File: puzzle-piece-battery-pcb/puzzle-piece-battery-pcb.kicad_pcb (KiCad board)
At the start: 2 copper layers, 27 x 27 mm, 18 parts, among them J1 Lipo, J2 INPUT, J3 OUTPUT, J4 GND Rivet, J5 5V Rivet, J6 3.3V Rivet, U2 MCP73831T-2ACI/OT, U3 LM3480-3.3

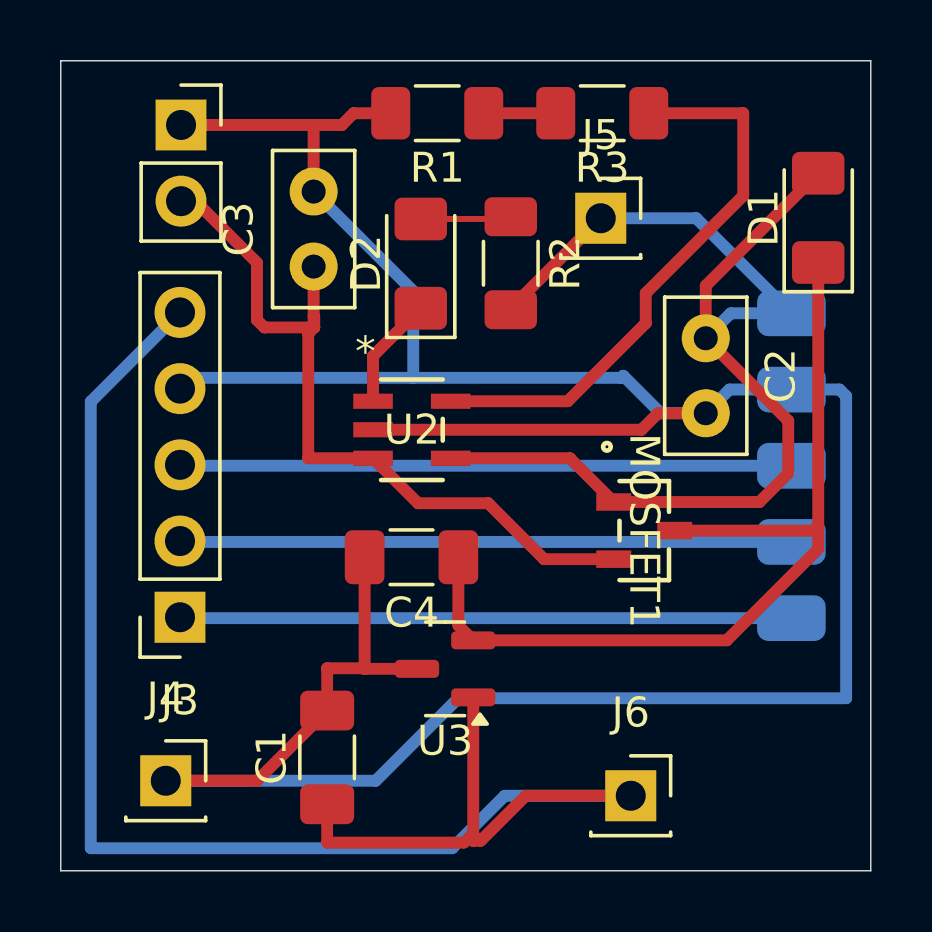
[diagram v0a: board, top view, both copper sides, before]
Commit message: made battery controller singled sided and removed lipo
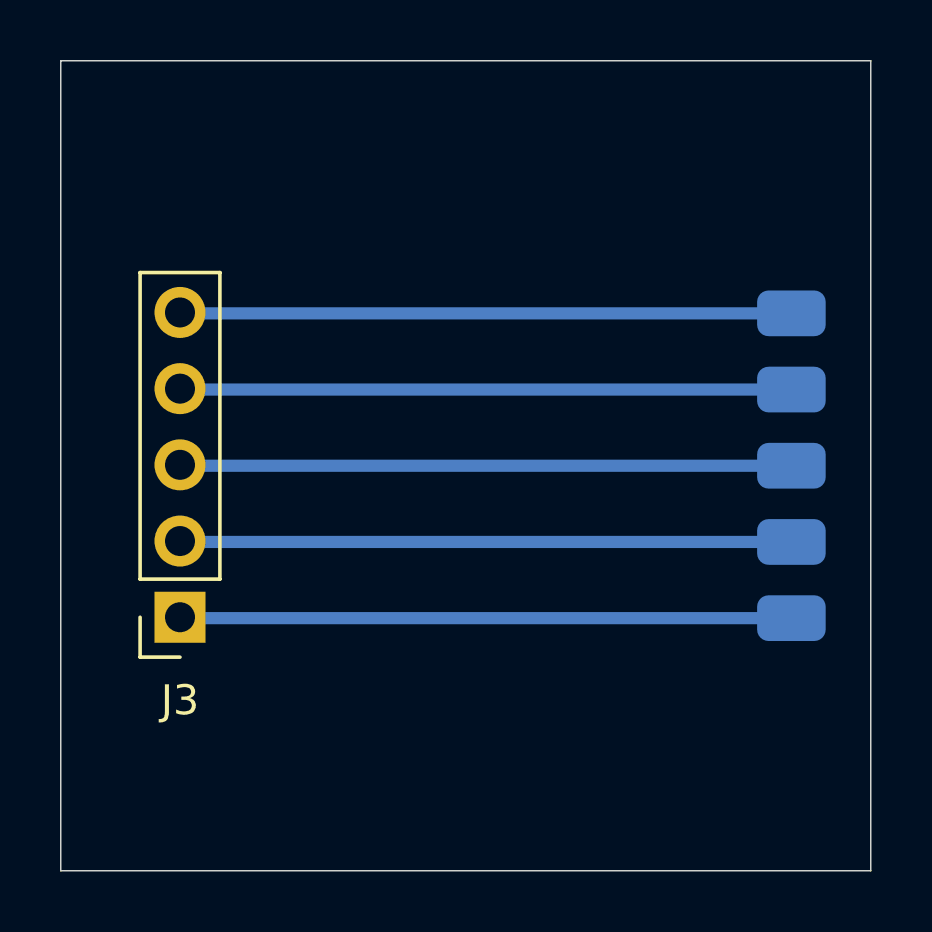
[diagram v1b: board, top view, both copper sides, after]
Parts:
- removed C1, C4: 0.1uF, Capacitor_SMD:C_1206_3216Metric_Pad1.33x1.80mm_HandSolder
- removed C2, C3: 4.7uF, Capacitor_THT:C_Disc_D5.0mm_W2.5mm_P2.50mm
- removed D1: D, Diode_SMD:D_1206_3216Metric_Pad1.42x1.75mm_HandSolder
- removed D2: LED, LED_SMD:LED_1206_3216Metric_Pad1.42x1.75mm_HandSolder
- removed J1: Lipo, Connector_PinSocket_2.54mm:PinSocket_1x02_P2.54mm_Vertical
- removed J4: GND Rivet, Connector_PinSocket_2.54mm:PinSocket_1x01_P2.54mm_Vertical
- removed J5: 5V Rivet, Connector_PinSocket_2.54mm:PinSocket_1x01_P2.54mm_Vertical
- removed J6: 3.3V Rivet, Connector_PinSocket_2.54mm:PinSocket_1x01_P2.54mm_Vertical
- removed MOSFET1: ZXM61P03FTA, ZXM61P03FTA:SOT23_ZETEX_DIO
- removed R1, R3: 10K, Resistor_SMD:R_1206_3216Metric_Pad1.30x1.75mm_HandSolder
- removed R2: 499, Resistor_SMD:R_1206_3216Metric_Pad1.30x1.75mm_HandSolder
- removed U2: MCP73831T-2ACI/OT, MCP73831T_2ACI_OT:SOT-23-5_MC_MCH
- removed U3: LM3480-3.3, Package_TO_SOT_SMD:SOT-23
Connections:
- J2 pad 5: +5V -> +3.3V
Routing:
- net GND: track 100.0 -> 20.4 mm
- net +5V: track 40.3 -> 0.00 mm
- net +3.3V: track 55.0 -> 20.4 mm
- net Net-(D1-K): track 30.1 -> 0.00 mm
- net VBAT: track 25.8 -> 0.00 mm
- net Net-(U2-PROG): track 19.1 -> 0.00 mm
- net STAT: track 3.76 -> 0.00 mm
- net Net-(D2-A): track 3.14 -> 0.00 mm
- net Net-(R1-Pad1): track 2.40 -> 0.00 mm

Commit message: add unrouted output throughholes to controller, and mounting holes
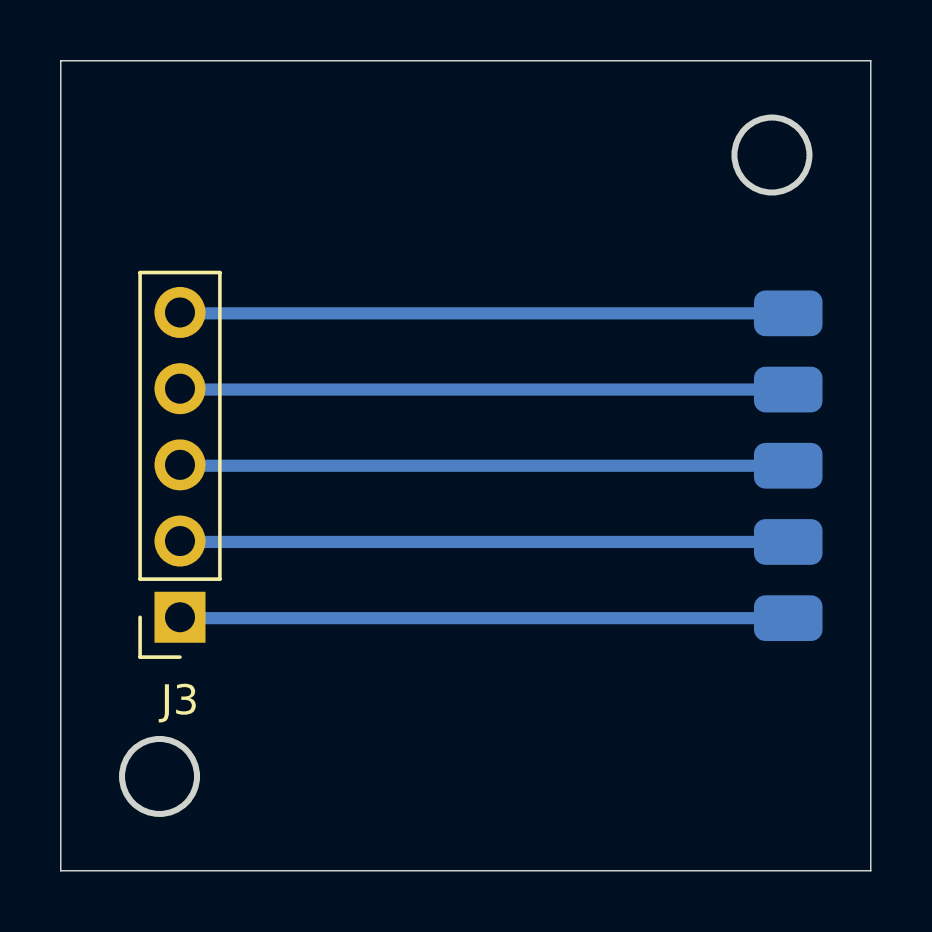
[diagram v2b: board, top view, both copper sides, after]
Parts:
- moved J2 0.10 mm to (186.8, 83.0)
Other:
- outline, holes or cut-outs redrawn
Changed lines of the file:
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@@
 		(allow_soldermask_bridges_in_footprints no)
 		(pcbplotparams
-			(layerselection 0x0001000_ffffffff)
+			(layerselection 0x0001000_fffffffe)
 			(plot_on_all_layers_selection 0x0000000_00000000)
 			(disableapertmacros no)
@@
 	(footprint "Connector_SMD:1x05_2.54mm_P"
 		(layer "B.Cu")
-		(at 186.855 83 90)
+		(at 186.75 83 90)
 		(property "Reference" "J2"
 			(at 0 6.81 -90)
@@
 		)
 	)
+	(gr_circle
+		(center 165.793 93.357)
+		(end 167.043 93.357)
+		(stroke
+			(width 0.2)
+			(type default)
+		)
+		(fill none)
+		(layer "Edge.Cuts")
+	)
+	(gr_circle
+		(center 186.207 72.643)
+		(end 187.457 72.643)
+		(stroke
+			(width 0.2)
+			(type default)
+		)
+		(fill none)
+		(layer "Edge.Cuts")
+	)
 	(gr_rect
 		(start 162.5 69.5)
@@
 		)
 		(height -0.5)
-		(gr_text "1062.9921 mils"
+		(gr_text "27.0000 mm"
 			(at 176 67.7 0)
 			(layer "F.SilkS")
@@
 		)
 		(height 0)
-		(gr_text "1062.9921 mils"
+		(gr_text "27.0000 mm"
 			(at 160.7 83 90)
 			(layer "F.SilkS")
